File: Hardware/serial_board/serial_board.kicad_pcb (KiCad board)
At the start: 2 copper layers, 80.8 x 60.1 mm, 11 parts, among them J1 Conn_01x40, J2 Conn_01x06, U1 W65C51NxP, X1 CXO_DIP8

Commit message: Many updates. SLOW signal is now shared amongst all slots, so their output has to be open drain.
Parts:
- added D1: LED, LED_SMD:LED_1206_3216Metric_Pad1.42x1.75mm_HandSolder, F.Cu at (33.7, -31.8)
- added D2: LED, LED_SMD:LED_1206_3216Metric_Pad1.42x1.75mm_HandSolder, F.Cu at (33.7, -36.1)
- added R1: R_Small, Resistor_SMD:R_0805_2012Metric_Pad1.15x1.40mm_HandSolder, B.Cu at (36.2, -31.8)
- added R2: R_Small, Resistor_SMD:R_0805_2012Metric_Pad1.15x1.40mm_HandSolder, B.Cu at (36.2, -36.1)
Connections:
- J1 pad 22: EX2 -> ~SLOW~
- J1 pad 42: EX3 -> CLK_12M
- J1 pad 44: EX4 -> EX2
- J1 pad 46: EX5 -> EX3
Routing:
- net Net-(D1-Pad2): track 47.1 -> 69.0 mm
- net Net-(D2-Pad2): track 50.7 -> 70.8 mm
- net Net-(D2-Pad1): vias 0 -> 1
- net Net-(D1-Pad1): vias 0 -> 1

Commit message: redo gerbers before ordering prototype boards
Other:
- board text added: "JLCJLCJLCJLC"

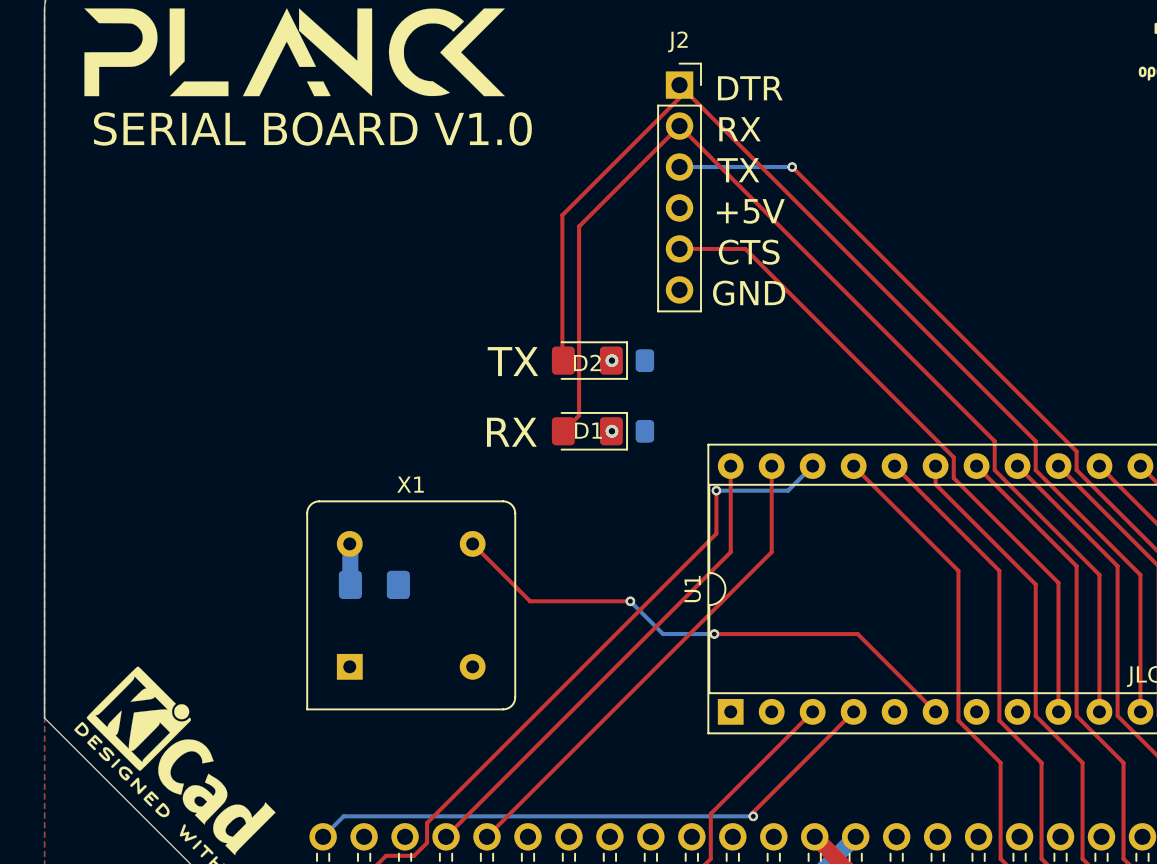
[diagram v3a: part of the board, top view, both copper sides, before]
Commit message: Add pullup on CS1 and move cts line to RTS of 6551
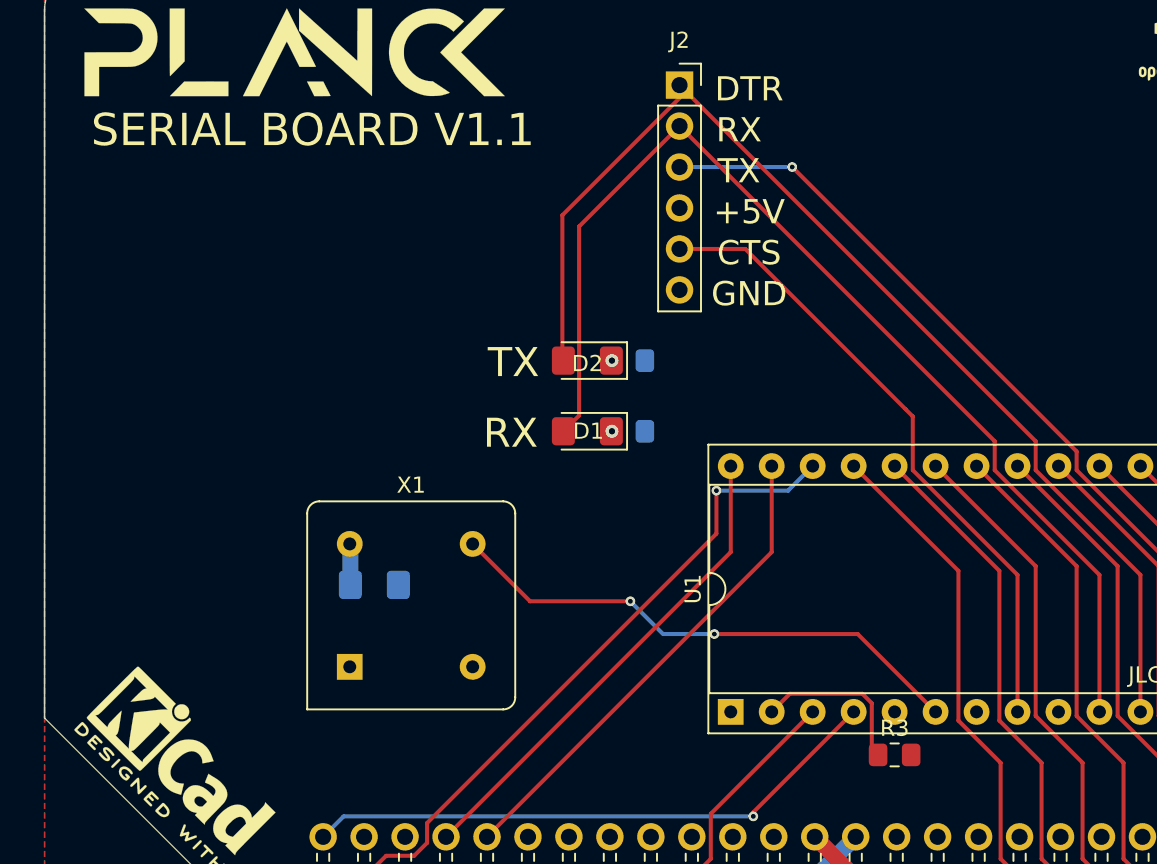
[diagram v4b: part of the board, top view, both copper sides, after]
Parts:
- added R3: 10k, Resistor_SMD:R_0805_2012Metric_Pad1.15x1.40mm_HandSolder, F.Cu at (52.7, -11.7)
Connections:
- U1 pad 8: Net-(U1-Pad8) -> Net-(J2-Pad5)
- U1 pad 9: Net-(J2-Pad5) -> Net-(U1-Pad9)
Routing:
- net Net-(R3-Pad1): track 0.00 -> 10.3 mm
- net Net-(J2-Pad5): track 40.8 -> 39.8 mm
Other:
- board text added: "SERIAL BOARD V1.1"
- board text removed: "SERIAL BOARD V1.0"

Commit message: small fixes on the hardware
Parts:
- moved D1 10.2 mm to (23.5, -32.0)
- moved D2 10.2 mm to (23.5, -36.4)
- moved R1 10.2 mm to (26.0, -32.0)
- moved R2 10.2 mm to (26.0, -36.4)
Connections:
- J2 pad 1: Net-(D2-Pad2) -> Net-(J2-Pad1)
- J2 pad 3: Net-(J2-Pad3) -> Net-(D2-Pad2)
- U1 pad 11: Net-(D2-Pad2) -> Net-(J2-Pad1)
- U1 pad 12: Net-(J2-Pad3) -> Net-(D2-Pad2)
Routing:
- net Net-(J2-Pad1): track 0.00 -> 51.5 mm
- net Net-(J2-Pad3): track 50.8 -> 0.00 mm, vias 1 -> 0
- net Net-(D1-Pad2): track 69.0 -> 78.0 mm
- net Net-(D2-Pad2): track 70.8 -> 73.6 mm, vias 0 -> 1
